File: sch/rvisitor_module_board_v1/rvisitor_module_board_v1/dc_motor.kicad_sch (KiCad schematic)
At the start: 32 parts, among them J1 Screw_Terminal_01x02, J2 Screw_Terminal_01x02, J3 Screw_Terminal_01x02, J4 Screw_Terminal_01x02, J5 ENC0, J6 ENC1, J7 ENC2, J8 ENC3, U2 L9110, U3 L9110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

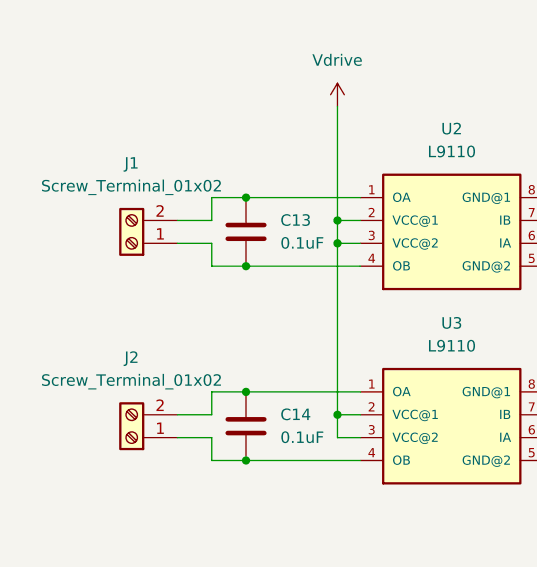
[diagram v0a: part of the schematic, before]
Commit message: [sch] rvisitor_module_board_v1 => power lines added
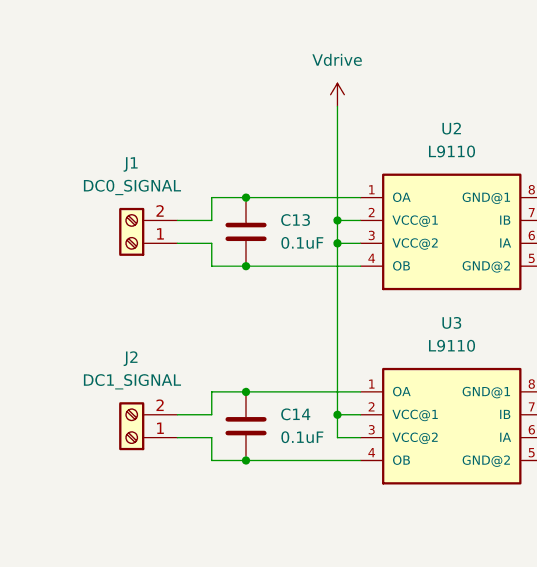
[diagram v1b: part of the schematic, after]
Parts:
- J1: value Screw_Terminal_01x02 -> DC0_SIGNAL
- J2: value Screw_Terminal_01x02 -> DC1_SIGNAL
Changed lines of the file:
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@@
       (effects (font (size 1.27 1.27)))
     )
-    (property "Value" "Screw_Terminal_01x02" (at 34.29 76.2 0)
+    (property "Value" "DC0_SIGNAL" (at 34.29 76.2 0)
       (effects (font (size 1.27 1.27)))
     )
@@
       (effects (font (size 1.27 1.27)))
     )
-    (property "Value" "Screw_Terminal_01x02" (at 34.29 97.79 0)
+    (property "Value" "DC1_SIGNAL" (at 34.29 97.79 0)
       (effects (font (size 1.27 1.27)))
     )

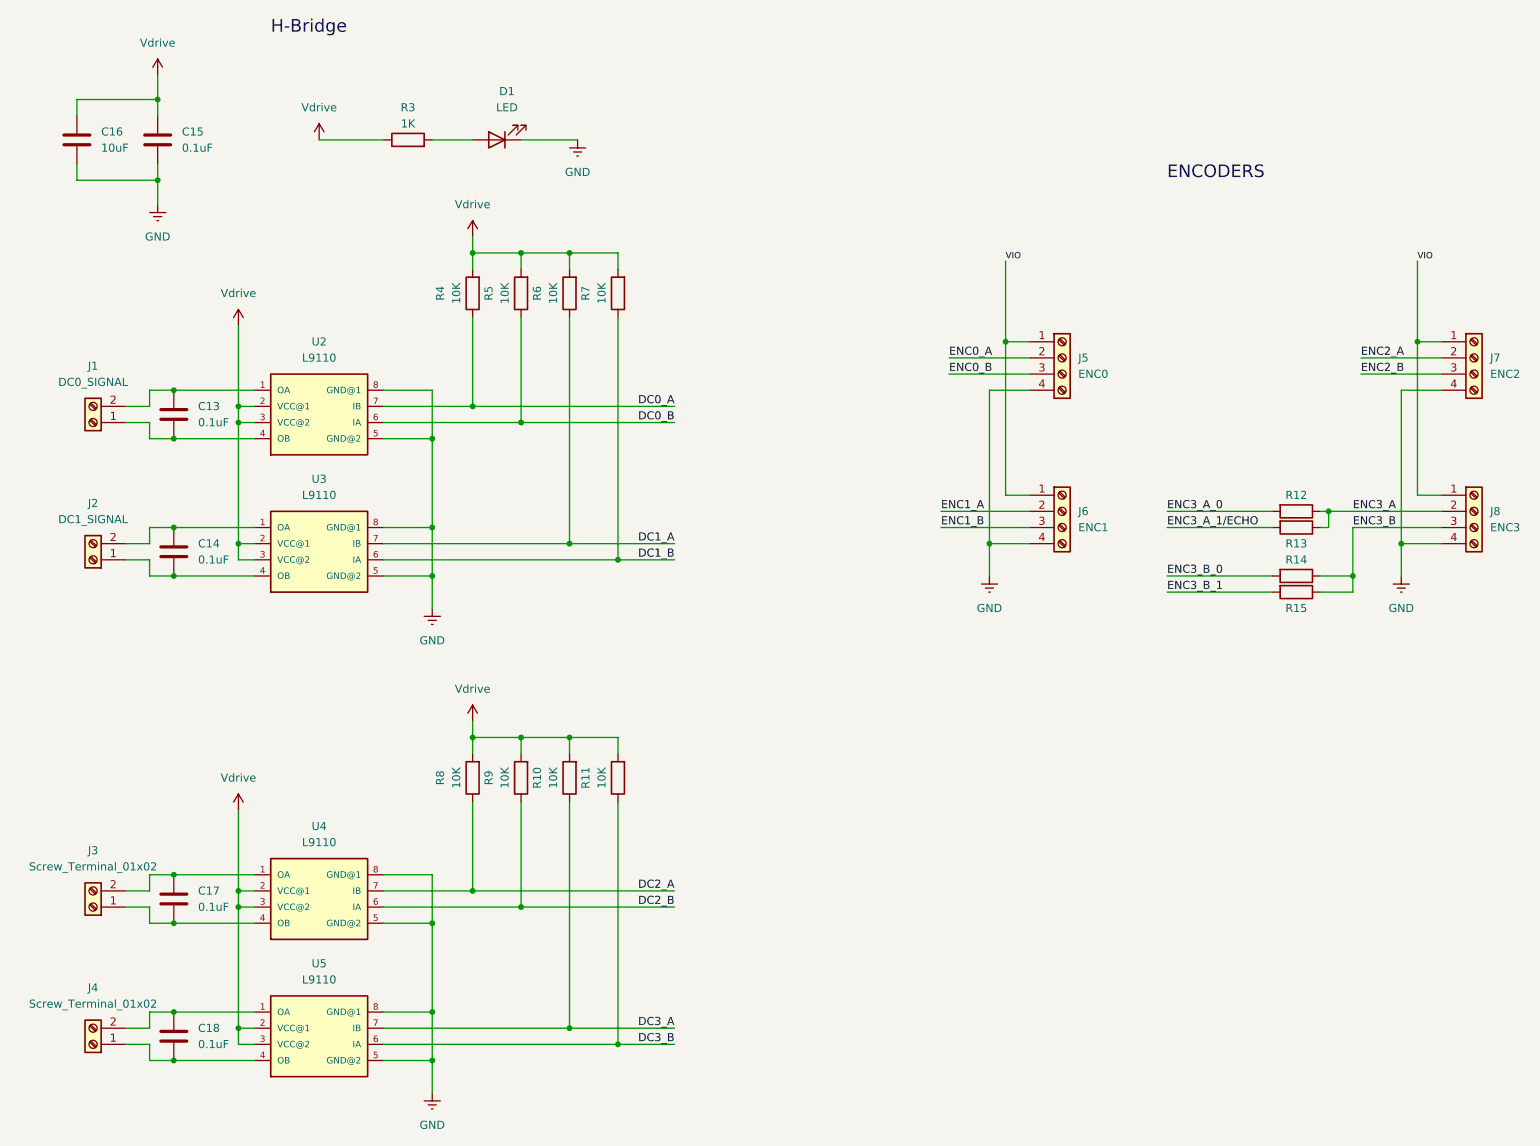
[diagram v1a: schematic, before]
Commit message: maket pcb start. maket add footprints. module_board_v1 start
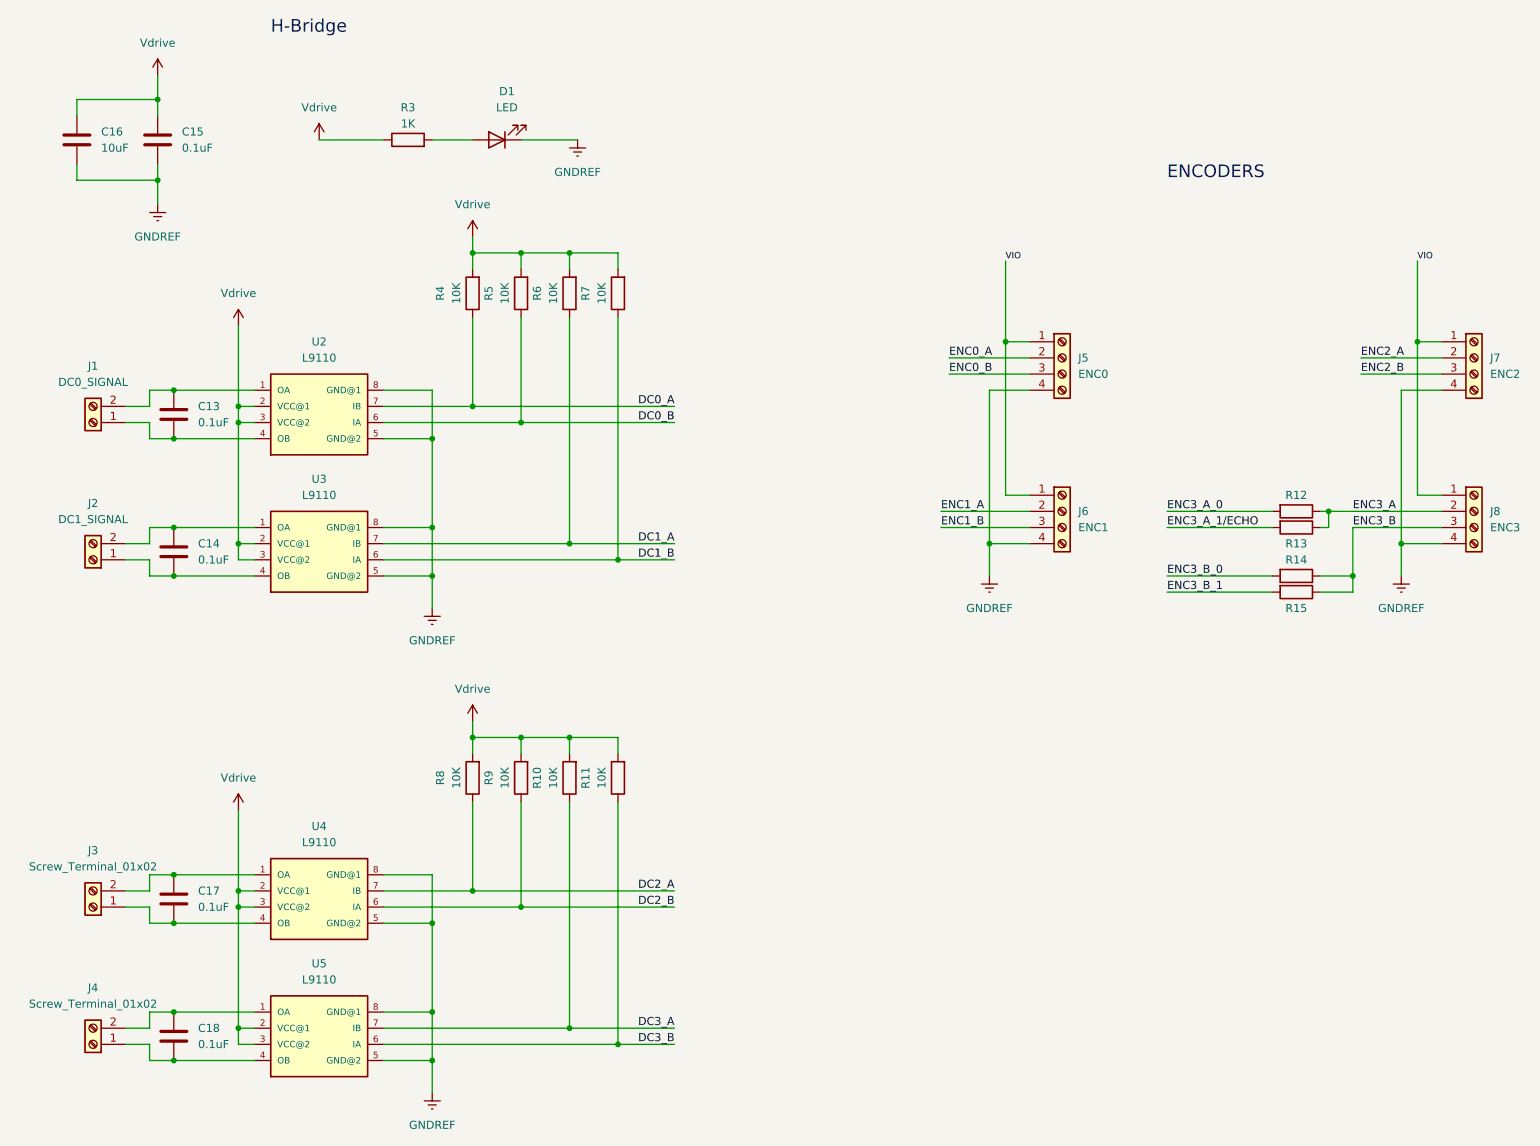
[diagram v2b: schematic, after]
